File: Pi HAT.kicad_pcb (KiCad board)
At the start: 2 copper layers, 65 x 41.5 mm, 89 parts, among them IC1 AD7730, J1 Screw_Terminal_01x04, J11 Conn_01x02_Male, J4 Barrel_Jack, J5 Screw_Terminal_01x03, J6 Screw_Terminal_01x03, J7 GPIO_CONNECTOR, J9 Conn_01x03_Male, K1 SANYOU_SRD_Form_C, K2 SANYOU_SRD_Form_C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

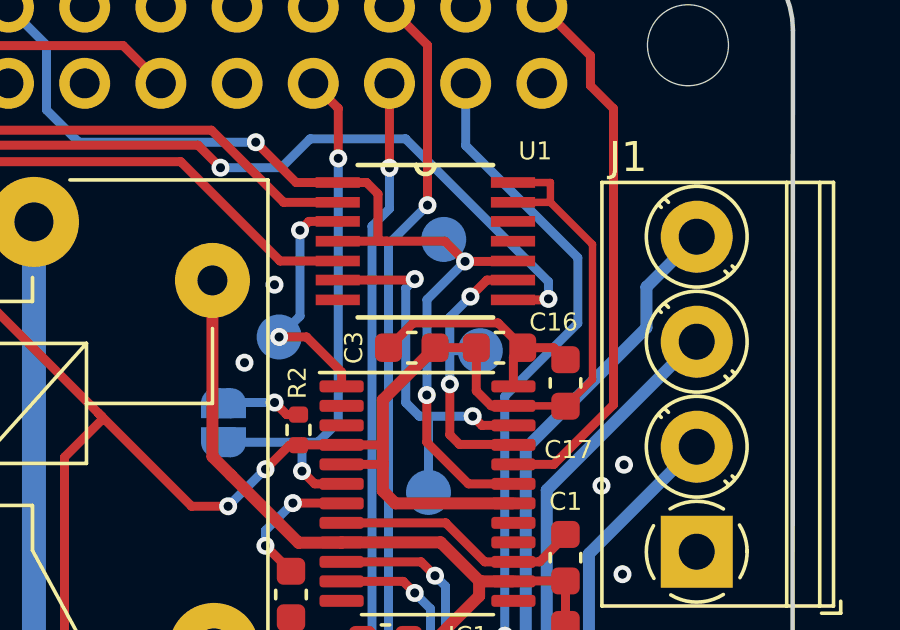
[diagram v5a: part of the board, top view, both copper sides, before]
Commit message: Silkscreen labelling
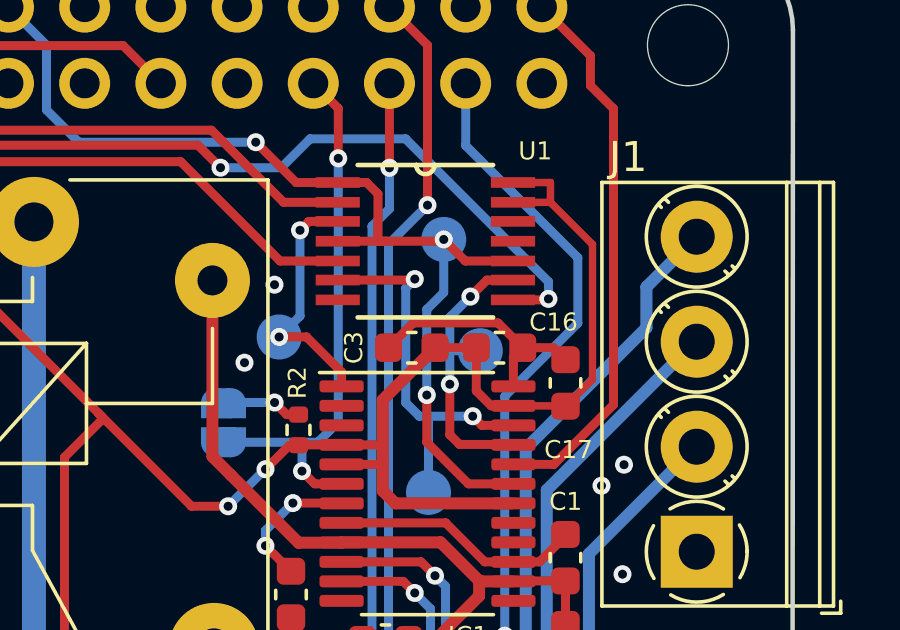
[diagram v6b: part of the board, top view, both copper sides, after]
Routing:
- net /GPIO7_SPI_CE1_N: track 35.2 -> 34.6 mm
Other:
- board text added: "!cs"
- board text added: "Default: 10SPS Bridge for 80SPS ODR"
- board text added: "Default: HX711 Break and bridge to use AD7730"
- board text added: "RPi0 Instrument. HAT v1.0.0 Montšo Mokake 09/12/2023"
- board text added: "miso"
- board text added: "mosi"
- board text added: "p/u !RST"
- board text added: "sck"
- board text removed: "RPi0 Instrument. HAT v0.0 Montso Mokake 18/12/2022"
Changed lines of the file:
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@@
     (property "ki_keywords" "test point tp")
     (attr exclude_from_pos_files)
-    (fp_text reference "TP7" (at 0 1.648) (layer "B.SilkS")
+    (fp_text reference "TP7" (at 0 1.648) (layer "B.SilkS") hide
         (effects (font (size 1 1) (thickness 0.15)) (justify mirror))
     )
@@
     (property "ki_keywords" "solder jumper SPST")
     (attr exclude_from_pos_files)
-    (fp_text reference "JP8" (at 0 1.8 90) (layer "B.SilkS")
+    (fp_text reference "JP8" (at 2.45 1.85 -180) (layer "B.SilkS")
         (effects (font (size 1 1) (thickness 0.15)) (justify mirror))
     )
@@
     (property "ki_keywords" "test point tp")
     (attr exclude_from_pos_files)
-    (fp_text reference "TP6" (at 0 1.648) (layer "B.SilkS")
+    (fp_text reference "TP6" (at 0 1.648) (layer "B.SilkS") hide
         (effects (font (size 1 1) (thickness 0.15)) (justify mirror))
     )
@@
     (property "ki_keywords" "test point tp")
     (attr exclude_from_pos_files)
-    (fp_text reference "TP8" (at 0 1.648) (layer "B.SilkS")
+    (fp_text reference "TP8" (at 0 1.648) (layer "B.SilkS") hide
         (effects (font (size 1 1) (thickness 0.15)) (justify mirror))
     )
@@
     (property "ki_keywords" "test point tp")
     (attr exclude_from_pos_files)
-    (fp_text reference "TP5" (at 2.6416 -0.3048) (layer "B.SilkS")
+    (fp_text reference "TP5" (at 2.6416 -0.3048) (layer "B.SilkS") hide
         (effects (font (size 1 1) (thickness 0.15)) (justify mirror))
     )
@@
   (gr_line (start 179.532 91.068) (end 120.532 91.068)
     (stroke (width 0.15) (type solid)) (layer "Edge.Cuts"))
-  (gr_text "RPi0 Instrument. HAT\nv0.0\nMontso Mokake\n18/12/2022" (at 157.48 121.5644) (layer "B.SilkS")
-    (effects (font (size 0.8 0.8) (thickness 0.13)) (justify mirror))
+  (gr_text "Default: 10SPS\nBridge for\n80SPS ODR" (at 180 130.95) (layer "B.SilkS")
+    (effects (font (size 0.8 0.8) (thickness 0.15)) (justify left bottom mirror))
+  )
+  (gr_text "Default: HX711\nBreak and bridge\nto use AD7730" (at 180.1 125.85) (layer "B.SilkS")
+    (effects (font (size 0.8 0.8) (thickness 0.15)) (justify left bottom mirror))
+  )
+  (gr_text "mosi" (at 175 109.95) (layer "B.SilkS")
+    (effects (font (size 1 1) (thickness 0.15)) (justify left bottom mirror))
+  )
+  (gr_text "sck" (at 169.1 104.8) (layer "B.SilkS")
+    (effects (font (size 1 1) (thickness 0.15)) (justify left bottom mirror))
+  )
+  (gr_text "miso" (at 176.85 105.25) (layer "B.SilkS")
+    (effects (font (size 1 1) (thickness 0.15)) (justify left bottom mirror))
+  )
+  (gr_text "!cs" (at 174.25 101.45) (layer "B.SilkS")
+    (effects (font (size 1 1) (thickness 0.15)) (justify left bottom mirror))
+  )
+  (gr_text "p/u !RST" (at 162.55 107.85) (layer "B.SilkS")
+    (effects (font (size 0.8 0.8) (thickness 0.15)) (justify left bottom mirror))
+  )
+  (gr_text "RPi0 Instrument. HAT\nv1.0.0\nMontšo Mokake\n09/12/2023" (at 153.85 122.5) (layer "B.SilkS")
+    (effects (font (size 1 1) (thickness 0.2) bold) (justify mirror))
   )
   (gr_text "Jumper" (at 127.56 122.72) (layer "Cmts.User")
@@
   (segment (start 130.72452 99.52548) (end 131.649906 98.600094) (width 0.3) (layer "B.Cu") (net 58))
   (segment (start 168.725 101.1) (end 169 101.1) (width 0.3) (layer "F.Cu") (net 59))
-  (segment (start 173.1854 101.775) (end 173.2 101.7604) (width 0.3) (layer "F.Cu") (net 59))
-  (segment (start 170.9274 101.1) (end 169 101.1) (width 0.3) (layer "F.Cu") (net 59))
+  (segment (start 170.8912 101.0412) (end 170.8324 101.1) (width 0.3) (layer "F.Cu") (net 59))
   (segment (start 168.3192 99.1442) (end 168.7 99.525) (width 0.3) (layer "F.Cu") (net 59))
   (segment (start 171.714 109.189) (end 173.2125 109.189) (width 0.3) (layer "F.Cu") (net 59))
   (segment (start 165.9692 99.1442) (end 167.358 99.1442) (width 0.3) (layer "F.Cu") (net 59))
   (segment (start 170.326511 106.228689) (end 170.326511 107.801511) (width 0.3) (layer "F.Cu") (net 59))
-  (segment (start 171.6024 101.775) (end 170.9274 101.1) (width 0.3) (layer "F.Cu") (net 59))
   (segment (start 168.7 101.075) (end 168.725 101.1) (width 0.3) (layer "F.Cu") (net 59))
+  (segment (start 171.6104 101.7604) (end 173.2 101.7604) (width 0.3) (layer "F.Cu") (net 59))
+  (segment (start 170.8324 101.1) (end 169 101.1) (width 0.3) (layer "F.Cu") (net 59))
   (segment (start 170.326511 107.801511) (end 171.714 109.189) (width 0.3) (layer "F.Cu") (net 59))
+  (segment (start 170.8912 101.0412) (end 171.6104 101.7604) (width 0.3) (layer "F.Cu") (net 59))
   (segment (start 167.358 101.1) (end 169 101.1) (width 0.3) (layer "F.Cu") (net 59))
   (segment (start 164.625 97.8) (end 165.9692 99.1442) (width 0.3) (layer "F.Cu") (net 59))
-  (segment (start 171.6024 101.775) (end 173.1854 101.775) (width 0.3) (layer "F.Cu") (net 59))
   (segment (start 168.7 99.525) (end 168.7 101.075) (width 0.3) (layer "F.Cu") (net 59))
   (segment (start 167.358 99.1442) (end 168.3192 99.1442) (width 0.3) (layer "F.Cu") (net 59))
   (via (at 170.326511 106.228689) (size 0.6) (drill 0.3) (layers "F.Cu" "B.Cu") (net 59))
-  (via (at 171.6024 101.775) (size 0.6) (drill 0.3) (layers "F.Cu" "B.Cu") (net 59))
+  (via (at 170.8912 101.0412) (size 0.6) (drill 0.3) (layers "F.Cu" "B.Cu") (net 59))
   (via (at 164.625 97.8) (size 0.6) (drill 0.3) (layers "F.Cu" "B.Cu") (net 59))
-  (segment (start 171.6024 101.7524) (end 170.8912 101.0412) (width 0.3) (layer "B.Cu") (net 59))
-  (segment (start 171.6024 101.775) (end 170.3324 103.045) (width 0.3) (layer "B.Cu") (net 59))
-  (segment (start 170.3324 103.045) (end 170.3324 106.2228) (width 0.3) (layer "B.Cu") (net 59))
-  (segment (start 171.6024 101.775) (end 171.6024 101.7524) (width 0.3) (layer "B.Cu") (net 59))
+  (segment (start 170.8912 101.0412) (end 170.8912 102.8088) (width 0.3) (layer "B.Cu") (net 59))
+  (segment (start 170.8912 102.8088) (end 170.326511 103.373489) (width 0.3) (layer "B.Cu") (net 59))
   (segment (start 157.65 96.725) (end 157.65 94.566) (width 0.3) (layer "B.Cu") (net 59))
   (segment (start 164.625 97.8) (end 158.725 97.8) (width 0.3) (layer "B.Cu") (net 59))
   (segment (start 158.725 97.8) (end 157.65 96.725) (width 0.3) (layer "B.Cu") (net 59))
-  (segment (start 170.3324 106.2228) (end 170.326511 106.228689) (width 0.3) (layer "B.Cu") (net 59))
+  (segment (start 170.326511 103.373489) (end 170.326511 106.228689) (width 0.3) (layer "B.Cu") (net 59))
   (segment (start 157.65 94.566) (end 156.382 93.298) (width 0.3) (layer "B.Cu") (net 59))
   (segment (start 166.589 109.189) (end 167.4875 109.189) (width 0.3) (layer "F.Cu") (net 63))

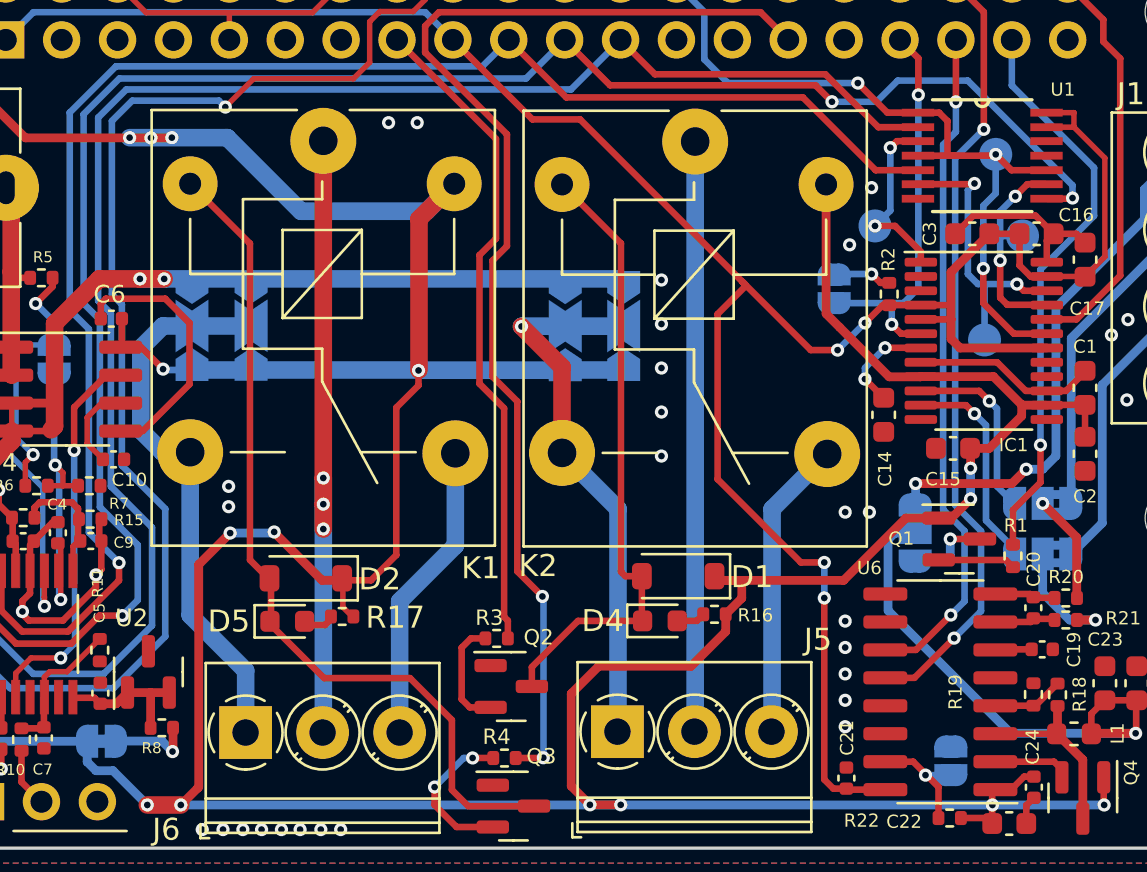
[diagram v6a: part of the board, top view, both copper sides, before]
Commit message: Connected power to relay COMs
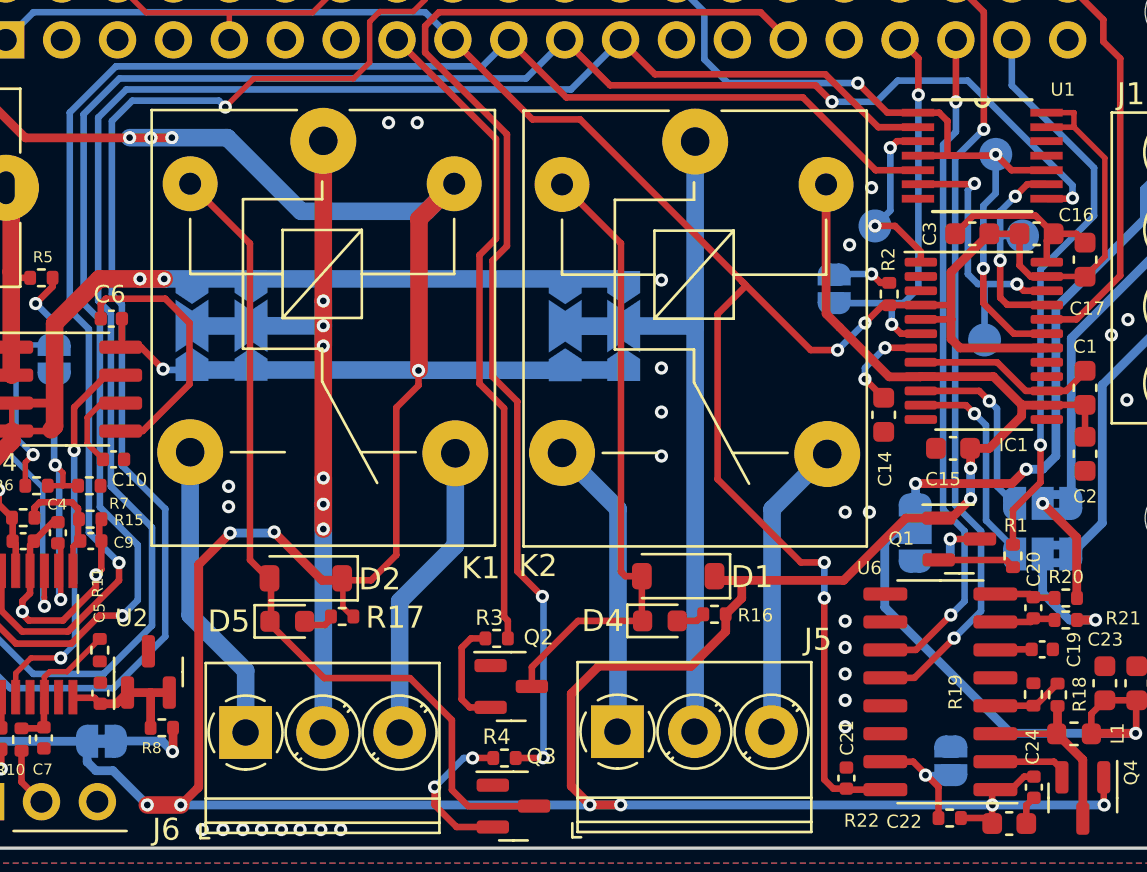
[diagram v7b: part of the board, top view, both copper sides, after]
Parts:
- added G***: LOGO, LOGO, B.Cu at (140.5, 119.2)
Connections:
- JP1 pad 2: /Relays/NO1 -> /Relays/COM1
- JP2 pad 2: /Relays/NO2 -> /Relays/COM2
- JP3 pad 2: /Relays/NO1 -> /Relays/COM1
- JP4 pad 2: /Relays/NO2 -> /Relays/COM2
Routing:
- net /Relays/NO2: track 25.5 -> 13.8 mm
- net /Relays/NO1: track 24.9 -> 13.7 mm, vias 1 -> 0
- net /Relays/COM2: track 29.2 -> 37.1 mm, vias 3 -> 6
- net /Relays/COM1: track 26.8 -> 32.7 mm
- net GND: vias 66 -> 65

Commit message: Fixed HX711 decoupling cap. Changed EXC+.
- Changed EXC+ to 4.06V
- Consistent values for schematic components
- Added B.silkscreen art
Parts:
- moved G*** 1.28 mm to (140.0, 120.5)
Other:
- board text removed: "p/u !RST"
